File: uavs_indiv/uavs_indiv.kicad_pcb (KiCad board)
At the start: 2 copper layers, 16 parts, among them J4 Conn_01x04_Pin, J5 Conn_01x04_Pin, J6 Conn_01x04_Pin, U1 LM2576HVS-5, U3 LM2576HVS-5

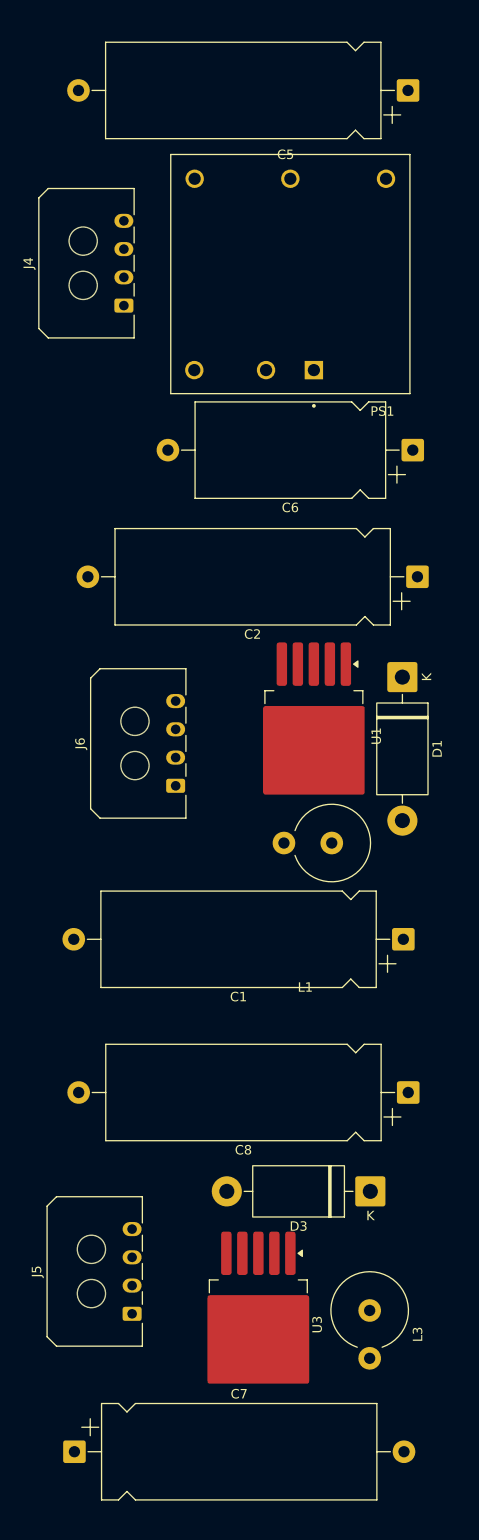
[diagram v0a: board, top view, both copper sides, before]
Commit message: added traces
join effort(95 - 5 split nikhil brian respectively)
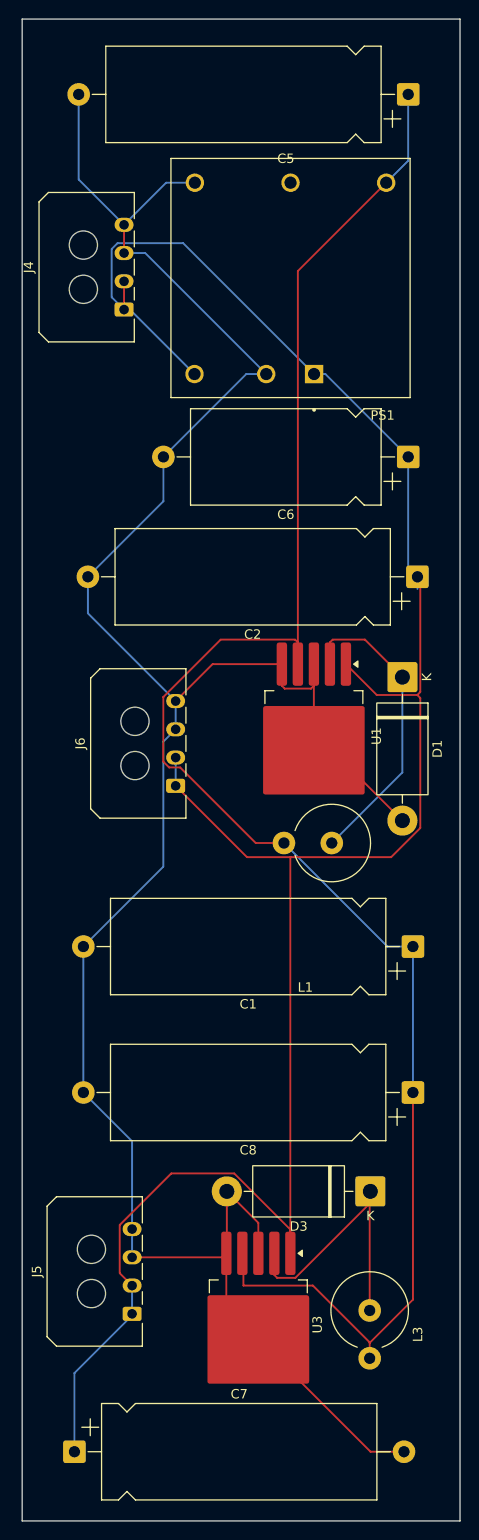
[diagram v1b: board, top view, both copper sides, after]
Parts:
- moved C1 1.28 mm to (147.0, 119.0)
- moved C6 0.87 mm to (146.5, 67.0)
- moved C8 0.50 mm to (147.0, 134.5)
- moved C5 0.42 mm to (146.5, 28.5)
- moved PS1 0.42 mm to (134.0, 48.0)
- moved J4 0.42 mm to (116.3, 51.4)
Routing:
- net GND: track 0.00 -> 260.3 mm
- net /Vin: track 0.00 -> 241.3 mm
- net +5V: track 0.00 -> 191.2 mm
- net Net-(D1-K): track 0.00 -> 34.2 mm
- net Net-(D3-K): track 0.00 -> 29.8 mm
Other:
- board outline added: 46.5 x 159.5 mm

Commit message: wtf did i just see
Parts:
- removed J4, J5: Conn_01x04_Pin, customdcdc:Molex_Micro-Fit_3.0_43650-0400_1x04_P3.00mm_Horizontal
- added J1: Conn_01x02_Socket, Connector_AMASS:AMASS_XT60PW-F_1x02_P7.20mm_Horizontal, F.Cu at (140.1, 126.5)
- moved C1 93.2 mm to (73.0, 62.3), turned to 0 degrees
- moved C5 92.9 mm to (73.0, 85.4), turned to 0 degrees
- moved C6 90.6 mm to (73.0, 120.0), turned to 0 degrees
- moved L3 86.8 mm to (141.7, 70.8), turned to 0 degrees
- moved C7 84.7 mm to (73.0, 96.9)
- moved C8 78.4 mm to (73.0, 108.5), turned to 0 degrees
- moved C2 74.7 mm to (73.0, 73.8), turned to 0 degrees
- moved D3 58.5 mm to (112.4, 94.8), turned to 0 degrees
- moved L1 46.9 mm to (141.7, 61.3), turned to 0 degrees
- moved U3 43.7 mm to (120.7, 116.7), turned to 0 degrees
- moved D1 33.6 mm to (112.4, 88.0), turned to 0 degrees
- moved PS1 25.5 mm to (123.5, 71.2), turned to 0 degrees
- moved U1 17.5 mm to (120.7, 104.3), turned to 0 degrees
- moved J6 12.0 mm to (132.1, 108.1), turned to 0 degrees
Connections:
- J6 pad 1: /Vin -> +5V
- J6 pad 2: /Vin -> +5V
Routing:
- net GND: track 260.3 -> 0.00 mm
- net /Vin: track 241.3 -> 0.00 mm
- net +5V: track 191.2 -> 0.00 mm
- net Net-(D1-K): track 34.2 -> 0.00 mm
- net Net-(D3-K): track 29.8 -> 0.00 mm
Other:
- board outline removed

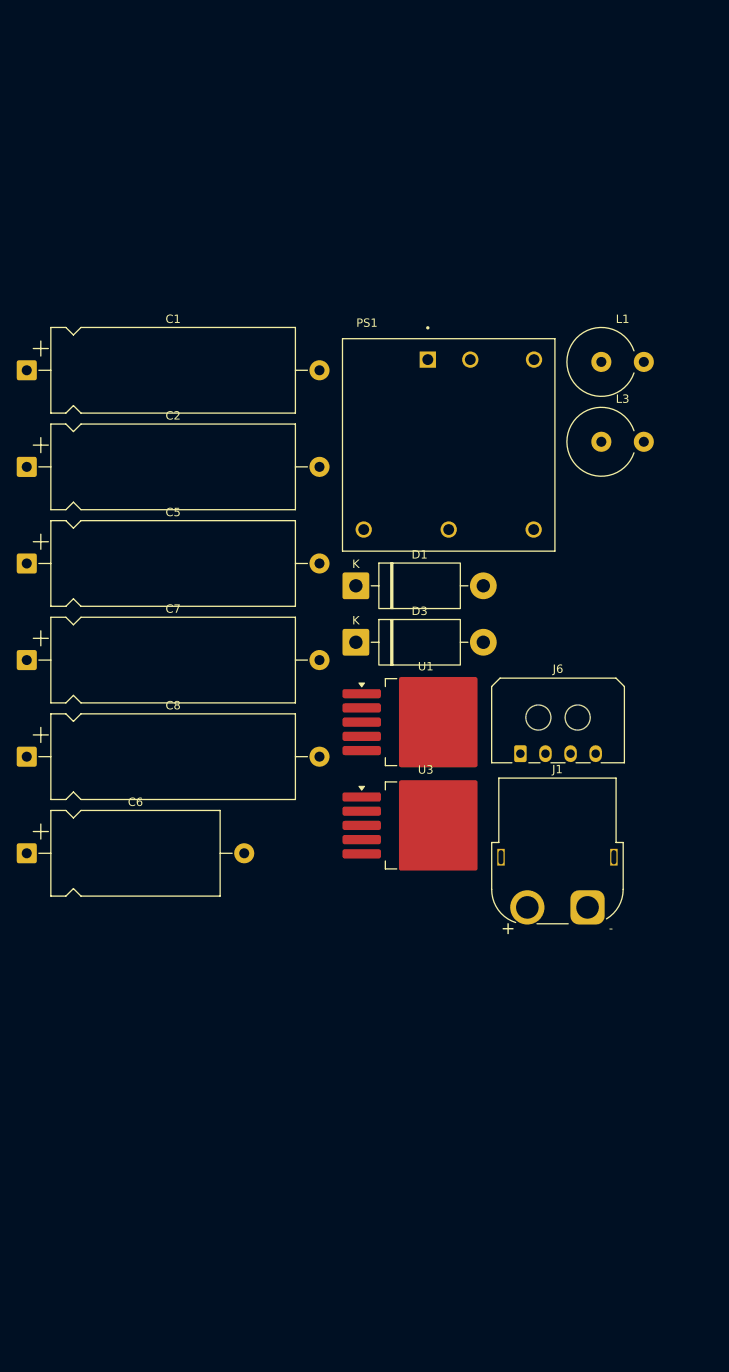
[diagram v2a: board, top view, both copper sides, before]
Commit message: added copper pours
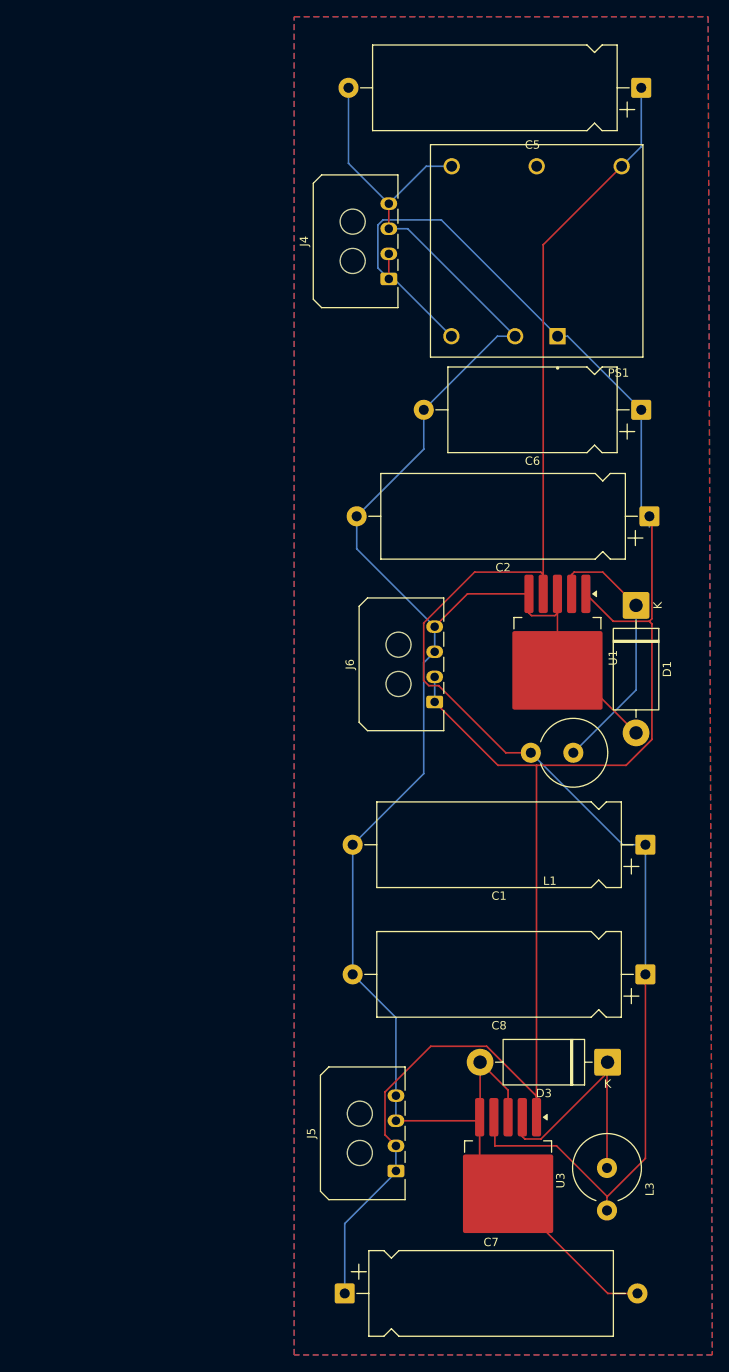
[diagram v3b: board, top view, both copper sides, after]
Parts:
- removed J1: Conn_01x02_Socket, Connector_AMASS:AMASS_XT60PW-F_1x02_P7.20mm_Horizontal
- added J4: Conn_01x04_Pin, customdcdc:Molex_Micro-Fit_3.0_43650-0400_1x04_P3.00mm_Horizontal, F.Cu at (116.3, 51.4)
- added J5: Conn_01x04_Pin, customdcdc:Molex_Micro-Fit_3.0_43650-0400_1x04_P3.00mm_Horizontal, F.Cu at (117.2, 158.0)
- moved C1 93.2 mm to (147.0, 119.0), turned to 180 degrees
- moved C5 92.9 mm to (146.5, 28.5), turned to 180 degrees
- moved C6 90.6 mm to (146.5, 67.0), turned to 180 degrees
- moved L3 86.8 mm to (142.4, 157.7), turned to -90 degrees
- moved C7 84.7 mm to (111.0, 172.7)
- moved C8 78.4 mm to (147.0, 134.5), turned to 180 degrees
- moved C2 74.7 mm to (147.5, 79.7), turned to 180 degrees
- moved D3 58.5 mm to (142.5, 145.0), turned to 180 degrees
- moved L1 46.9 mm to (138.4, 108.0), turned to 180 degrees
- moved U3 43.7 mm to (130.6, 159.2), turned to -90 degrees
- moved D1 33.6 mm to (145.9, 90.4), turned to -90 degrees
- moved PS1 25.5 mm to (134.0, 48.0), turned to 180 degrees
- moved U1 17.5 mm to (136.5, 96.7), turned to -90 degrees
- moved J6 12.0 mm to (121.8, 101.9), turned to 90 degrees
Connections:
- J6 pad 1: +5V -> /Vin
- J6 pad 2: +5V -> /Vin
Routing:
- net GND: track 0.00 -> 260.3 mm
- net /Vin: track 0.00 -> 241.3 mm
- net +5V: track 0.00 -> 191.2 mm
- net Net-(D1-K): track 0.00 -> 34.2 mm
- net Net-(D3-K): track 0.00 -> 29.8 mm
- added copper zone on B.Cu, net GND
- added copper zone on F.Cu, net GND

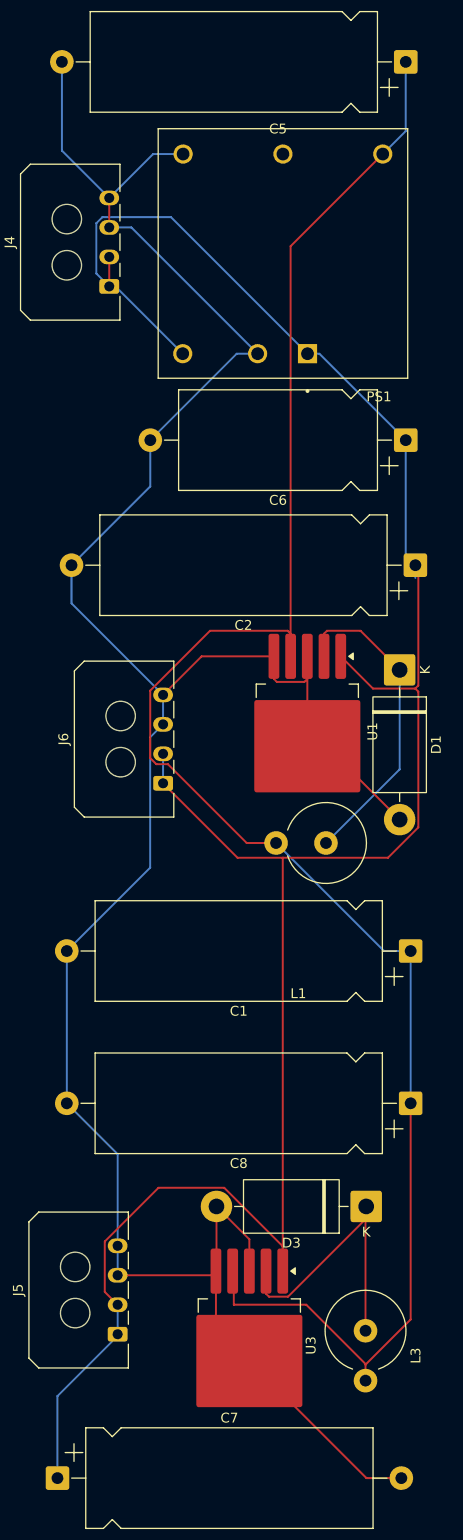
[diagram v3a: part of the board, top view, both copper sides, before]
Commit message: got rid of copper pours, added via, got rid of ground routing, fixed silkscreen
wip:
adding edge cuts board
changing the thickness of the traces for power pours
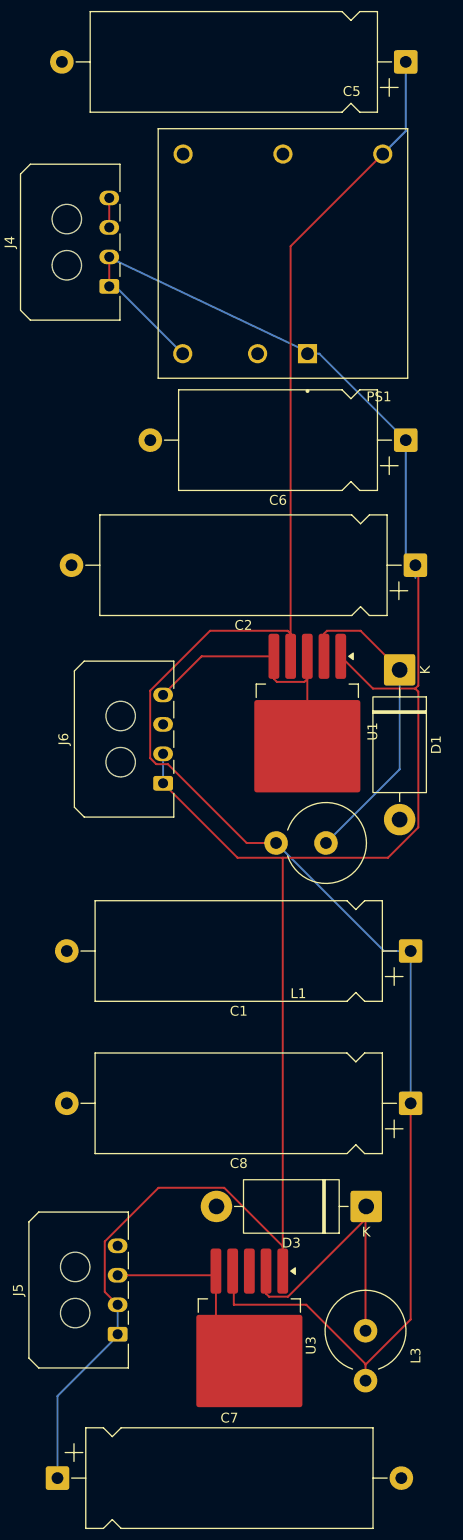
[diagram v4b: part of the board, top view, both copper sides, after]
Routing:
- net GND: track 260.3 -> 57.6 mm, vias 0 -> 16
- net /Vin: track 241.3 -> 206.9 mm

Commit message: redidt footprints and routing
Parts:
- removed J4, J5: Conn_01x04_Pin, customdcdc:Molex_Micro-Fit_3.0_43650-0400_1x04_P3.00mm_Horizontal
- added J1: Conn_01x02_Socket, Connector_AMASS:AMASS_XT60PW-F_1x02_P7.20mm_Horizontal, F.Cu at (174.6, 42.1)
- added J2: Conn_01x04_Pin, customdcdc:Molex_Micro-Fit_3.0_43650-0400_1x04_P3.00mm_Horizontal, F.Cu at (144.2, 71.7)
- added J3: Conn_01x04_Pin, customdcdc:Molex_Micro-Fit_3.0_43650-0400_1x04_P3.00mm_Horizontal, F.Cu at (202.0, 71.5)
- C1, C8: value 330uF -> 1000uF; footprint Capacitor_THT:CP_Axial_L29.0mm_D10.0mm_P35.00mm_Horizontal -> customdcdc:capacitor1000uf
- C2, C7: footprint Capacitor_THT:CP_Axial_L29.0mm_D10.0mm_P35.00mm_Horizontal -> customdcdc:capacitor100uf
- C5: footprint Capacitor_THT:CP_Axial_L29.0mm_D10.0mm_P35.00mm_Horizontal -> customdcdc:capacitor220uf
- C6: footprint Capacitor_THT:CP_Axial_L20.0mm_D10.0mm_P26.00mm_Horizontal -> customdcdc:capacitor680uf
- L1, L3: value 330u -> 100u; footprint Inductor_THT:L_Axial_L20.0mm_D8.0mm_P5.08mm_Vertical -> customdcdc:inductor3.5a100u
- moved C7 135.1 mm to (151.5, 43.8)
- moved U3 110.3 mm to (160.4, 53.0), turned to 0 degrees
- moved L3 95.4 mm to (157.6, 63.5), turned to 180 degrees
- moved D3 94.1 mm to (147.5, 51.0)
- moved PS1 86.5 mm to (220.0, 57.5), turned to 0 degrees
- moved C5 78.1 mm to (209.5, 74.6), turned to 0 degrees
- moved U1 76.4 mm to (199.2, 53.0), turned to 0 degrees
- moved C6 76.2 mm to (217.2, 38.6), turned to 0 degrees
- moved C8 75.6 mm to (137.5, 59.5)
- moved L1 73.0 mm to (197.0, 64.5)
- moved C1 64.6 mm to (172.2, 59.5), turned to 0 degrees
- moved J6 62.9 mm to (176.7, 71.2), turned to 180 degrees
- moved D1 56.3 mm to (186.1, 51.0), turned to 180 degrees
- moved C2 55.9 mm to (190.0, 43.5), turned to 0 degrees
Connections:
- J6 pad 1: /Vin -> +5V
- J6 pad 2: /Vin -> +5V
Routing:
- net /Vin: track 206.9 -> 104.4 mm
- net +5V: track 191.2 -> 149.7 mm
- net GND: track 57.6 -> 25.4 mm, vias 16 -> 10
- net Net-(D1-K): track 34.2 -> 21.8 mm
- net Net-(D3-K): track 29.8 -> 20.9 mm
- removed copper zone on F.Cu, net GND
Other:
- board outline added: 105 x 56 mm
- board text added: "why havent u started yet dumbass"

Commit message: changed vin traces and added name
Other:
- board text added: "Nikhil Gummadidala"
- board text removed: "why havent u started yet dumbass"
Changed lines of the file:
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@@
 		(layer "Edge.Cuts")
 	)
-	(gr_text "why havent u started yet dumbass"
-		(at -1245.5 -173.5 0)
-		(layer "F.Cu")
+	(gr_text "Nikhil Gummadidala"
+		(at 219 28 0)
+		(layer "F.SilkS")
 		(effects
 			(font
-				(size 100 100)
-				(thickness 20)
-				(bold yes)
+				(size 1 1)
+				(thickness 0.1)
 			)
 			(justify left bottom)
@@
 		)
 	)
+	(group ""
+		(members "22140ed1-756e-41a4-9d49-fbdfd35b7d6a" "23d31e87-93ed-4e0a-9616-89849535bec7"
+			"2b7d7a1a-4a32-49a8-8cfa-6527cc26b4a0" "2fe9e073-72a5-4aed-a92e-d5b4c162e45b"
+			"4bf6b008-ff5a-4964-aaf0-0080f85656c0" "4e5911f0-c088-4619-8884-d1f3c3af7060"
+			"564f98f7-52d9-46e6-a810-7242e843f151" "5d988a54-7c61-43c2-b00a-2fd897df1714"
+			"5fa07a42-df69-4905-aeda-c575929e9b95" "84a5b02e-e3cc-4577-8c86-8c9cbcecb784"
+			"959fda9b-2020-44f8-8151-f95f94510a31" "96b29b8e-8289-43cb-a1a5-b40429c5e14c"
+			"9949c927-d1ee-428a-827d-9d41e442d9fe" "99eab567-5164-4258-9b0a-c1d4163fa726"
+			"9aa1177d-9894-47e0-9754-030981c918ed" "c683ee58-d7c7-45cd-b983-6164c2c6c8b4"
+			"c919fed8-55a1-48de-8cdf-6dfacc3b540f" "cf1ae832-df63-4838-bb96-79eb712def17"
+			"e61e609f-35d9-417d-ae65-22742d10c756"
+		)
+	)
